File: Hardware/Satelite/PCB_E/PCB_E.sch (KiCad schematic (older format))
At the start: 15 parts, among them J1 Conn_02x02_Counter_Clockwise, J12 Conector_Expansion_CanSat, J14 Conn_01x06, J15 Conn_01x06, J2 Conn_02x02_Counter_Clockwise, J3 Conn_02x02_Counter_Clockwise, J4 Conn_02x10_Odd_Even, J5 Conn_02x10_Odd_Even, J6 Conn_02x10_Odd_Even, J7 Conn_02x10_Odd_Even, J8 Conn_01x04, M1 Spacer, M2 Spacer, M3 Spacer

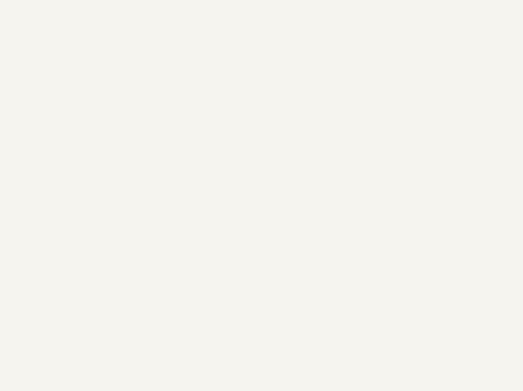
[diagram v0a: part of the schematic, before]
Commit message: Logo open hardware en esquemáticos
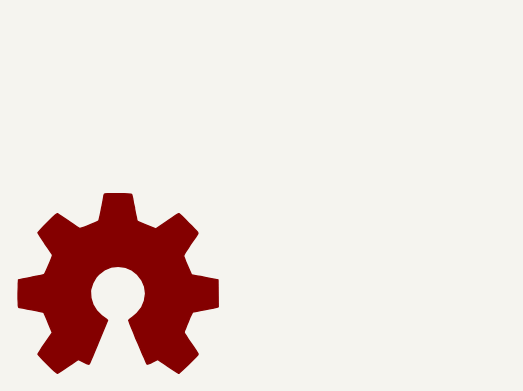
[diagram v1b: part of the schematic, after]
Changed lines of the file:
@@
 Text Label 9650 4600 0    50   ~ 0
 Vbus
+$Comp
+L Graphic:Logo_Open_Hardware_Large #LOGO?
+U 1 1 5C333B8B
+P 1200 7200
+F 0 "#LOGO?" H 1200 7700 50  0001 C CNN
+F 1 "Logo_Open_Hardware_Large" H 1200 6800 50  0001 C CNN
+F 2 "" H 1200 7200 50  0001 C CNN
+F 3 "~" H 1200 7200 50  0001 C CNN
+	1    1200 7200
+	1    0    0    -1
+$EndComp
 $EndSCHEMATC
